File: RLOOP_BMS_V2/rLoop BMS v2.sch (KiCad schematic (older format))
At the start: 2 parts

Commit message: Footprint work
starting to assign footprints to parts
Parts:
- R3, R4: footprint (none) -> Resistors_SMD:R_0603
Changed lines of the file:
@@
 F 0 "R3" V 6100 2550 50  0000 C CNN
 F 1 "10R / 0.125W / 1% / SMD 0603" V 6300 2800 50  0000 C CNN
-F 2 "" V 6130 2600 50  0001 C CNN
+F 2 "Resistors_SMD:R_0603" V 6130 2600 50  0001 C CNN
 F 3 "" H 6200 2600 50  0001 C CNN
 	1    6200 2600
@@
 F 0 "R4" V 6100 4450 50  0000 C CNN
 F 1 "10R / 0.125W / 1% / SMD 0603" V 6300 5050 50  0000 C CNN
-F 2 "" V 6130 4500 50  0001 C CNN
+F 2 "Resistors_SMD:R_0603" V 6130 4500 50  0001 C CNN
 F 3 "" H 6200 4500 50  0001 C CNN
 	1    6200 4500

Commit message: more PCB layout work
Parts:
- added R95: 10R / 0.125W / 1% / SMD 0603, Resistors_SMD:R_0603, symbol R
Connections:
- net Batt Conn/Cell_0: now also R95.1
- new net CONTROLLER 1/GND: R95.2
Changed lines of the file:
@@
 	10150 1500 9200 1500
-Wire Wire Line
-	9200 1500 9200 1600
 Wire Wire Line
 	9200 1600 10150 1600
@@
 Connection ~ 9900 2600
 Wire Wire Line
-	6000 7200 6900 7200
-Wire Wire Line
 	6900 7200 6900 6350
 Wire Wire Line
@@
 	6050 2350 6050 2900
 Connection ~ 6050 2600
+$Comp
+L R R95
+U 1 1 591DF6A5
+P 6450 7200
+F 0 "R95" V 6350 7150 50  0000 C CNN
+F 1 "10R / 0.125W / 1% / SMD 0603" V 6550 7000 50  0000 C CNN
+F 2 "Resistors_SMD:R_0603" V 6380 7200 50  0001 C CNN
+F 3 "" H 6450 7200 50  0001 C CNN
+	1    6450 7200
+	0    1    1    0
+$EndComp
+Wire Wire Line
+	6000 7200 6300 7200
+Wire Wire Line
+	6600 7200 6900 7200
 $EndSCHEMATC

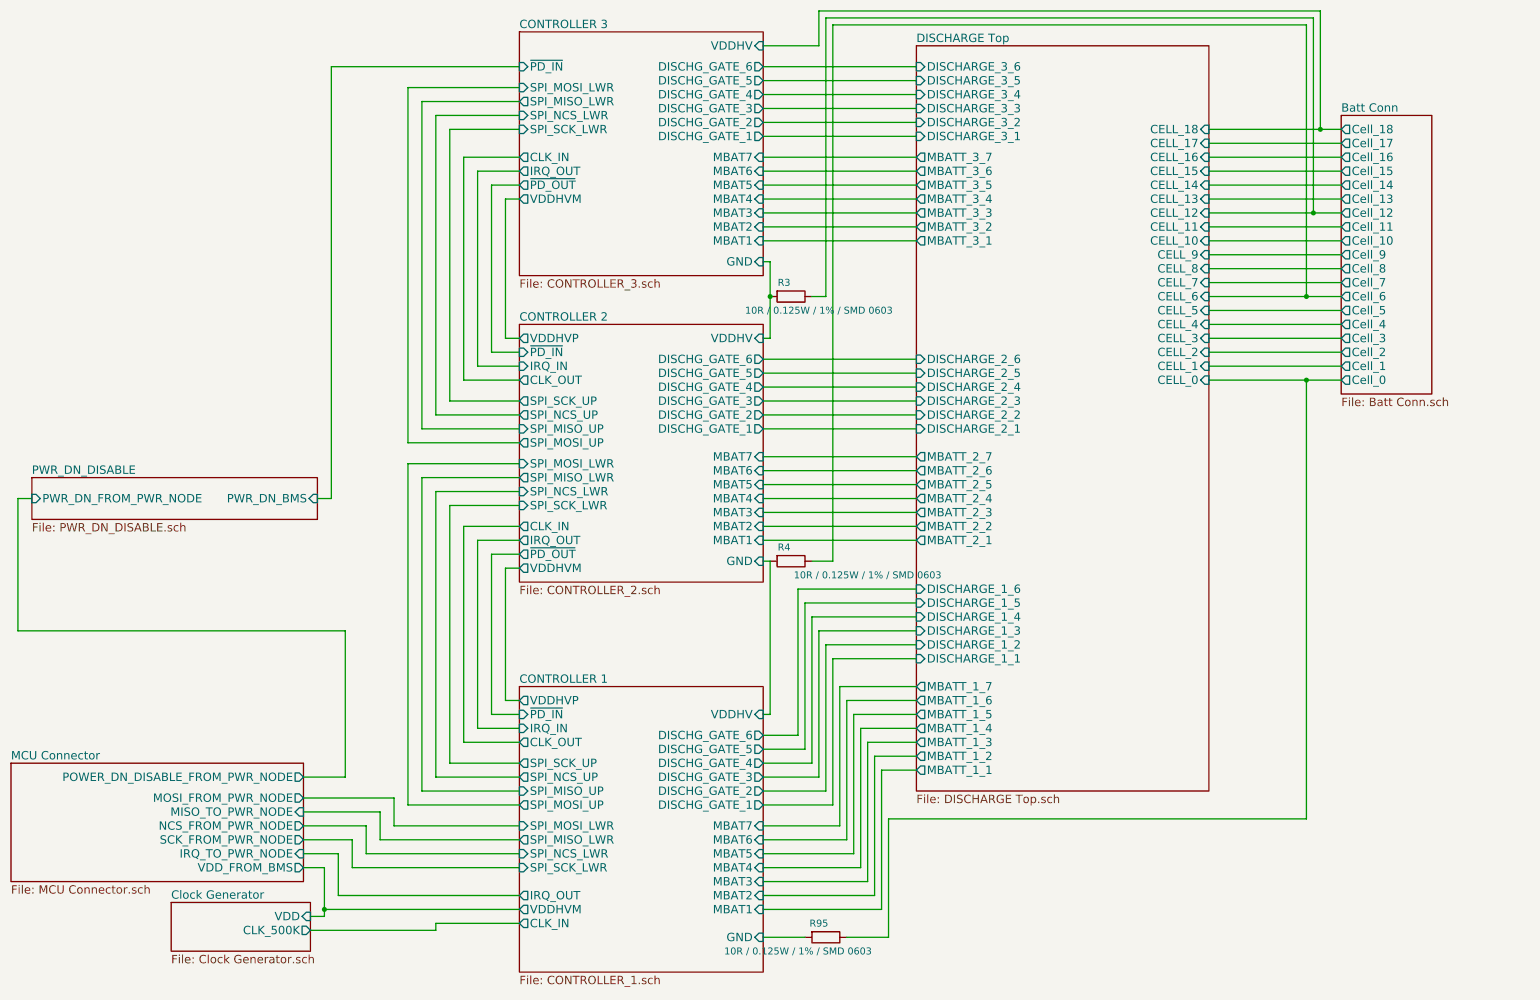
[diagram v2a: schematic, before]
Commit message: WIP
See if it's even possible
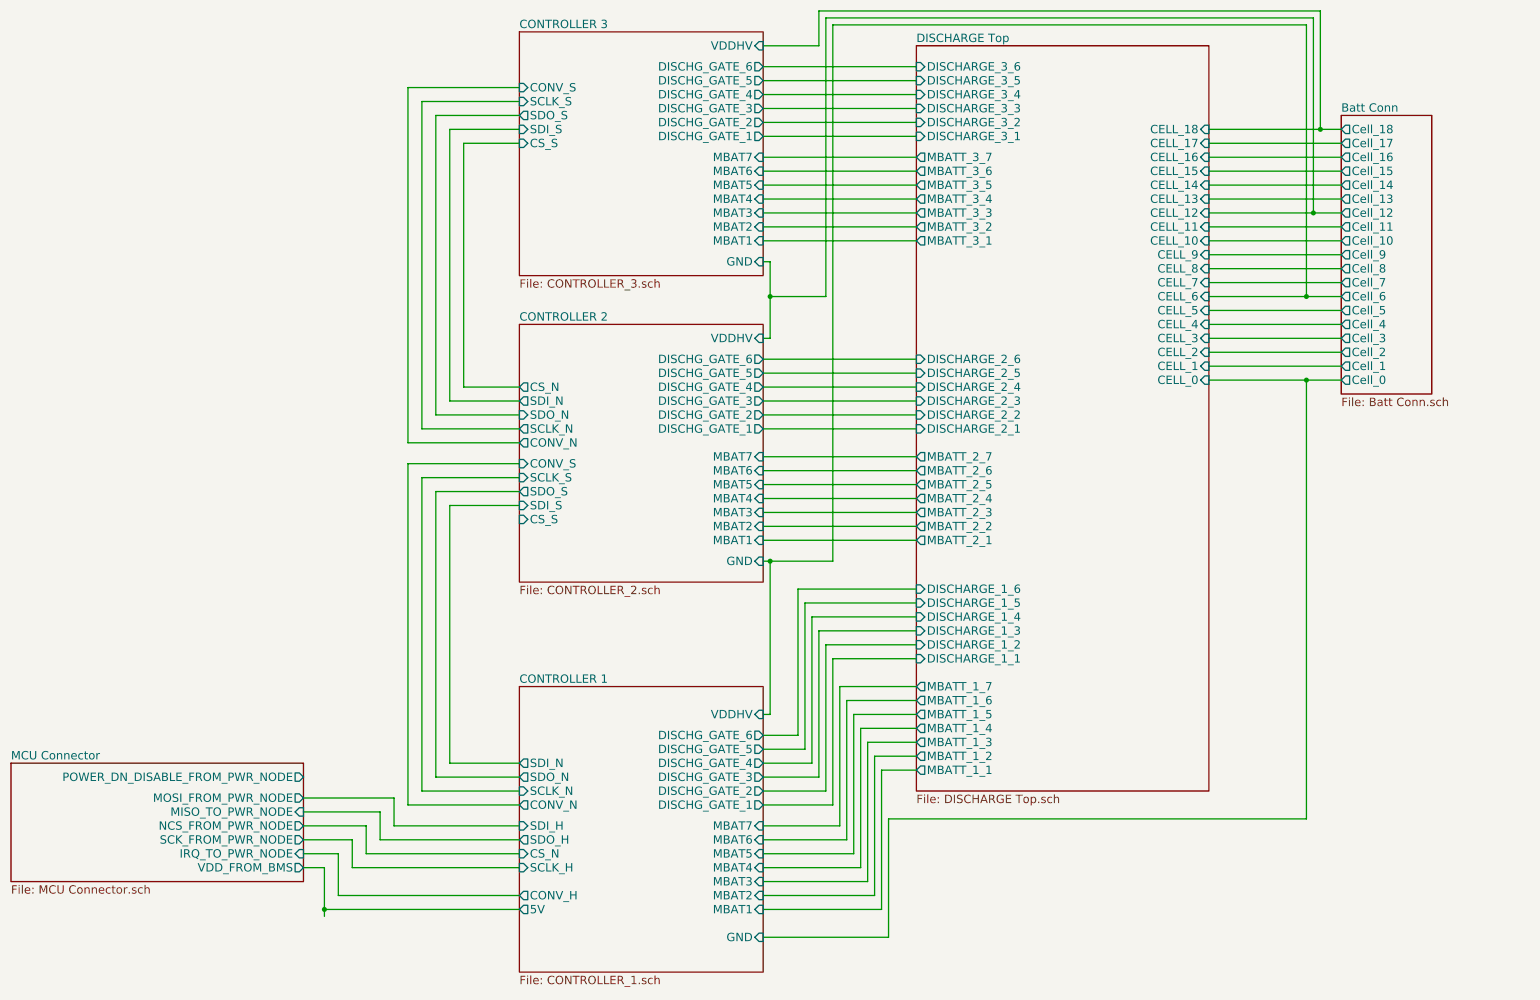
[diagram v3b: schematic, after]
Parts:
- removed R3, R4, R95: 10R / 0.125W / 1% / SMD 0603, Resistors_SMD:R_0603, symbol R
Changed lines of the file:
@@
 $Descr A4 11693 8268
 encoding utf-8
-Sheet 1 9
+Sheet 1 7
 Title ""
 Date ""
@@
 Comment4 ""
 $EndDescr
-$Sheet
-S 1750 6950 1000 350
-U 590C13C3
-F0 "Clock Generator" 60
-F1 "Clock Generator.sch" 60
-F2 "CLK_500K" O R 2750 7150 60
-F3 "VDD" I R 2750 7050 60
-$EndSheet
 $Sheet
 S 600  5950 2100 850
@@
 F7 "POWER_DN_DISABLE_FROM_PWR_NODE" O R 2700 6050 60
 F8 "VDD_FROM_BMS" O R 2700 6700 60
-$EndSheet
-$Sheet
-S 750  3900 2050 300
-U 590C2114
-F0 "PWR_DN_DISABLE" 60
-F1 "PWR_DN_DISABLE.sch" 60
-F2 "PWR_DN_FROM_PWR_NODE" I L 750 4050 60
-F3 "PWR_DN_BMS" I R 2800 4050 60
 $EndSheet
 $Sheet
@@
 F19 "Cell_17" O L 10150 1500 60
 F20 "Cell_18" O L 10150 1400 60
-$EndSheet
-$Sheet
-S 4250 2800 1750 1850
-U 590D87FF
-F0 "CONTROLLER 2" 60
-F1 "CONTROLLER_2.sch" 60
-F2 "MBAT1" I R 6000 4350 60
-F3 "MBAT2" I R 6000 4250 60
-F4 "MBAT3" I R 6000 4150 60
-F5 "MBAT4" I R 6000 4050 60
-F6 "MBAT5" I R 6000 3950 60
-F7 "MBAT6" I R 6000 3850 60
-F8 "MBAT7" I R 6000 3750 60
-F9 "DISCHG_GATE_1" O R 6000 3550 60
-F10 "DISCHG_GATE_2" O R 6000 3450 60
-F11 "DISCHG_GATE_3" O R 6000 3350 60
-F12 "DISCHG_GATE_4" O R 6000 3250 60
-F13 "DISCHG_GATE_5" O R 6000 3150 60
-F14 "DISCHG_GATE_6" O R 6000 3050 60
-F15 "~PD_IN" I L 4250 3000 60
-F16 "~PD_OUT" O L 4250 4450 60
-F17 "CLK_IN" O L 4250 4250 60
-F18 "CLK_OUT" O L 4250 3200 60
-F19 "SPI_NCS_LWR" I L 4250 4000 60
-F20 "SPI_SCK_LWR" I L 4250 4100 60
-F21 "SPI_MOSI_LWR" I L 4250 3800 60
-F22 "SPI_MISO_LWR" O L 4250 3900 60
-F23 "IRQ_IN" I L 4250 3100 60
-F24 "IRQ_OUT" O L 4250 4350 60
-F25 "SPI_MISO_UP" I L 4250 3550 60
-F26 "SPI_SCK_UP" O L 4250 3350 60
-F27 "SPI_NCS_UP" O L 4250 3450 60
-F28 "VDDHVM" O L 4250 4550 60
-F29 "VDDHVP" O L 4250 2900 60
-F30 "SPI_MOSI_UP" O L 4250 3650 60
-F31 "VDDHV" I R 6000 2900 60
-F32 "GND" I R 6000 4500 60
-$EndSheet
-$Sheet
-S 4250 5400 1750 2050
-U 590D88AD
-F0 "CONTROLLER 1" 60
-F1 "CONTROLLER_1.sch" 60
-F2 "MBAT1" I R 6000 7000 60
-F3 "MBAT2" I R 6000 6900 60
-F4 "MBAT3" I R 6000 6800 60
-F5 "MBAT4" I R 6000 6700 60
-F6 "MBAT5" I R 6000 6600 60
-F7 "MBAT6" I R 6000 6500 60
-F8 "MBAT7" I R 6000 6400 60
-F9 "DISCHG_GATE_1" O R 6000 6250 60
-F10 "DISCHG_GATE_2" O R 6000 6150 60
-F11 "DISCHG_GATE_3" O R 6000 6050 60
-F12 "DISCHG_GATE_4" O R 6000 5950 60
-F13 "DISCHG_GATE_5" O R 6000 5850 60
-F14 "DISCHG_GATE_6" O R 6000 5750 60
-F15 "~PD_IN" I L 4250 5600 60
-F16 "CLK_IN" O L 4250 7100 60
-F17 "CLK_OUT" O L 4250 5800 60
-F18 "SPI_NCS_LWR" I L 4250 6600 60
-F19 "SPI_SCK_LWR" I L 4250 6700 60
-F20 "SPI_MOSI_LWR" I L 4250 6400 60
-F21 "SPI_MISO_LWR" O L 4250 6500 60
-F22 "IRQ_IN" I L 4250 5700 60
-F23 "IRQ_OUT" O L 4250 6900 60
-F24 "SPI_MISO_UP" I L 4250 6150 60
-F25 "SPI_SCK_UP" O L 4250 5950 60
-F26 "SPI_NCS_UP" O L 4250 6050 60
-F27 "VDDHVP" O L 4250 5500 60
-F28 "SPI_MOSI_UP" O L 4250 6250 60
-F29 "VDDHVM" O L 4250 7000 60
-F30 "VDDHV" I R 6000 5600 60
-F31 "GND" I R 6000 7200 60
-$EndSheet
-$Sheet
-S 4250 700  1750 1750
-U 590C6B15
-F0 "CONTROLLER 3" 60
-F1 "CONTROLLER_3.sch" 60
-F2 "MBAT1" I R 6000 2200 60
-F3 "MBAT2" I R 6000 2100 60
-F4 "MBAT3" I R 6000 2000 60
-F5 "MBAT4" I R 6000 1900 60
-F6 "MBAT5" I R 6000 1800 60
-F7 "MBAT6" I R 6000 1700 60
-F8 "MBAT7" I R 6000 1600 60
-F9 "DISCHG_GATE_1" O R 6000 1450 60
-F10 "DISCHG_GATE_2" O R 6000 1350 60
-F11 "DISCHG_GATE_3" O R 6000 1250 60
-F12 "DISCHG_GATE_4" O R 6000 1150 60
-F13 "DISCHG_GATE_5" O R 6000 1050 60
-F14 "DISCHG_GATE_6" O R 6000 950 60
-F15 "~PD_IN" I L 4250 950 60
-F16 "~PD_OUT" O L 4250 1800 60
-F17 "CLK_IN" O L 4250 1600 60
-F18 "SPI_NCS_LWR" I L 4250 1300 60
-F19 "SPI_SCK_LWR" I L 4250 1400 60
-F20 "SPI_MOSI_LWR" I L 4250 1100 60
-F21 "SPI_MISO_LWR" O L 4250 1200 60
-F22 "IRQ_OUT" O L 4250 1700 60
-F23 "VDDHVM" O L 4250 1900 60
-F24 "VDDHV" I R 6000 800 60
-F25 "GND" I R 6000 2350 60
 $EndSheet
 $Sheet
@@
 F59 "CELL_18" I R 9200 1400 60
 $EndSheet
-$Comp
-L R R3
-U 1 1 59153F46
-P 6200 2600
-F 0 "R3" V 6100 2550 50  0000 C CNN
-F 1 "10R / 0.125W / 1% / SMD 0603" V 6300 2800 50  0000 C CNN
-F 2 "Resistors_SMD:R_0603" V 6130 2600 50  0001 C CNN
-F 3 "" H 6200 2600 50  0001 C CNN
-	1    6200 2600
-	0    1    1    0
-$EndComp
-$Comp
-L R R4
-U 1 1 59158071
-P 6200 4500
-F 0 "R4" V 6100 4450 50  0000 C CNN
-F 1 "10R / 0.125W / 1% / SMD 0603" V 6300 5050 50  0000 C CNN
-F 2 "Resistors_SMD:R_0603" V 6130 4500 50  0001 C CNN
-F 3 "" H 6200 4500 50  0001 C CNN
-	1    6200 4500
-	0    1    1    0
-$EndComp
-Wire Wire Line
-	4250 2900 4150 2900
-Wire Wire Line
-	4150 2900 4150 1900
-Wire Wire Line
-	4150 1900 4250 1900
-Wire Wire Line
-	4250 3000 4050 3000
-Wire Wire Line
-	4050 3000 4050 1800
-Wire Wire Line
-	4050 1800 4250 1800
-Wire Wire Line
-	4250 3100 3950 3100
-Wire Wire Line
-	3950 3100 3950 1700
-Wire Wire Line
-	3950 1700 4250 1700
 Wire Wire Line
 	3750 1400 4250 1400
 Wire Wire Line
-	4250 1600 3850 1600
-Wire Wire Line
-	3850 1600 3850 3200
-Wire Wire Line
-	3850 3200 4250 3200
-Wire Wire Line
 	4250 3350 3750 3350
 Wire Wire Line
@@
 	3450 3650 4250 3650
 Wire Wire Line
-	4250 950  2900 950
-Wire Wire Line
-	2900 950  2900 4050
-Wire Wire Line
-	2900 4050 2800 4050
-Wire Wire Line
-	4250 5500 4150 5500
-Wire Wire Line
-	4150 5500 4150 4550
-Wire Wire Line
-	4150 4550 4250 4550
-Wire Wire Line
-	4250 5600 4050 5600
-Wire Wire Line
-	4050 5600 4050 4450
-Wire Wire Line
-	4050 4450 4250 4450
-Wire Wire Line
-	4250 5700 3950 5700
-Wire Wire Line
-	3950 5700 3950 4350
-Wire Wire Line
-	3950 4350 4250 4350
-Wire Wire Line
-	4250 5800 3850 5800
-Wire Wire Line
-	3850 5800 3850 4250
-Wire Wire Line
-	3850 4250 4250 4250
-Wire Wire Line
 	3750 5950 4250 5950
 Wire Wire Line
@@
 	3350 6200 2700 6200
 Wire Wire Line
-	2700 6050 3000 6050
-Wire Wire Line
-	3000 6050 3000 5000
-Wire Wire Line
-	3000 5000 650  5000
-Wire Wire Line
-	650  5000 650  4050
-Wire Wire Line
-	650  4050 750  4050
-Wire Wire Line
 	9200 1400 10150 1400
 Wire Wire Line
@@
 	7100 2200 6000 2200
 Wire Wire Line
-	6000 4500 6050 4500
+	6000 4500 6500 4500
 Wire Wire Line
 	6050 4500 6050 5600
@@
 Connection ~ 10000 1400
 Wire Wire Line
-	6350 2600 6450 2600
+	6050 2600 6450 2600
 Wire Wire Line
 	6450 2600 6450 600
 Wire Wire Line
 	6450 600  9950 600
-Wire Wire Line
-	6350 4500 6500 4500
 Wire Wire Line
 	6500 4500 6500 650
@@
 	9950 600  9950 2000
 Connection ~ 9950 2000
-Wire Wire Line
-	2850 7050 2750 7050
 Connection ~ 2850 7000
-Wire Wire Line
-	2750 7150 3650 7150
-Wire Wire Line
-	3650 7150 3650 7100
-Wire Wire Line
-	3650 7100 4250 7100
 Wire Wire Line
 	6050 2350 6050 2900
 Connection ~ 6050 2600
-$Comp
-L R R95
-U 1 1 591DF6A5
-P 6450 7200
-F 0 "R95" V 6350 7150 50  0000 C CNN
-F 1 "10R / 0.125W / 1% / SMD 0603" V 6550 7000 50  0000 C CNN
-F 2 "Resistors_SMD:R_0603" V 6380 7200 50  0001 C CNN
-F 3 "" H 6450 7200 50  0001 C CNN
-	1    6450 7200
-	0    1    1    0
-$EndComp
-Wire Wire Line
-	6000 7200 6300 7200
-Wire Wire Line
-	6600 7200 6900 7200
+Wire Wire Line
+	6000 7200 6900 7200
+Connection ~ 6050 4500
+$Sheet
+S 4250 700  1750 1750
+U 590C6B15
+F0 "CONTROLLER 3" 60
+F1 "CONTROLLER_3.sch" 60
+F2 "MBAT1" I R 6000 2200 60
+F3 "MBAT2" I R 6000 2100 60
+F4 "MBAT3" I R 6000 2000 60
+F5 "MBAT4" I R 6000 1900 60
+F6 "MBAT5" I R 6000 1800 60
+F7 "MBAT6" I R 6000 1700 60
+F8 "MBAT7" I R 6000 1600 60
+F9 "DISCHG_GATE_1" O R 6000 1450 60
+F10 "DISCHG_GATE_2" O R 6000 1350 60
+F11 "DISCHG_GATE_3" O R 6000 1250 60
+F12 "DISCHG_GATE_4" O R 6000 1150 60
+F13 "DISCHG_GATE_5" O R 6000 1050 60
+F14 "DISCHG_GATE_6" O R 6000 950 60
+F15 "CS_S" I L 4250 1500 60
+F16 "SDO_S" O L 4250 1300 60
+F17 "SDI_S" I L 4250 1400 60
+F18 "CONV_S" I L 4250 1100 60
+F19 "SCLK_S" I L 4250 1200 60
+F20 "VDDHV" I R 6000 800 60
+F21 "GND" I R 6000 2350 60
+$EndSheet
+$Sheet
+S 4250 2800 1750 1850
+U 590D87FF
+F0 "CONTROLLER 2" 60
+F1 "CONTROLLER_2.sch" 60
+F2 "MBAT1" I R 6000 4350 60
+F3 "MBAT2" I R 6000 4250 60
+F4 "MBAT3" I R 6000 4150 60
+F5 "MBAT4" I R 6000 4050 60
+F6 "MBAT5" I R 6000 3950 60
+F7 "MBAT6" I R 6000 3850 60
+F8 "MBAT7" I R 6000 3750 60
+F9 "DISCHG_GATE_1" O R 6000 3550 60
+F10 "DISCHG_GATE_2" O R 6000 3450 60
+F11 "DISCHG_GATE_3" O R 6000 3350 60
+F12 "DISCHG_GATE_4" O R 6000 3250 60
+F13 "DISCHG_GATE_5" O R 6000 3150 60
+F14 "DISCHG_GATE_6" O R 6000 3050 60
+F15 "SDO_S" O L 4250 4000 60
+F16 "SDI_S" I L 4250 4100 60
+F17 "CONV_S" I L 4250 3800 60
+F18 "SCLK_S" I L 4250 3900 60
+F19 "SCLK_N" O L 4250 3550 60
+F20 "SDI_N" O L 4250 3350 60
+F21 "SDO_N" I L 4250 3450 60
+F22 "CONV_N" O L 4250 3650 60
+F23 "VDDHV" I R 6000 2900 60
+F24 "GND" I R 6000 4500 60
+F25 "CS_S" I L 4250 4200 60
+F26 "CS_N" O L 4250 3250 60
+$EndSheet
+$Sheet
+S 4250 5400 1750 2050
+U 590D88AD
+F0 "CONTROLLER 1" 60
+F1 "CONTROLLER_1.sch" 60
+F2 "MBAT1" I R 6000 7000 60
+F3 "MBAT2" I R 6000 6900 60
+F4 "MBAT3" I R 6000 6800 60
+F5 "MBAT4" I R 6000 6700 60
+F6 "MBAT5" I R 6000 6600 60
+F7 "MBAT6" I R 6000 6500 60
+F8 "MBAT7" I R 6000 6400 60
+F9 "DISCHG_GATE_1" O R 6000 6250 60
+F10 "DISCHG_GATE_2" O R 6000 6150 60
+F11 "DISCHG_GATE_3" O R 6000 6050 60
+F12 "DISCHG_GATE_4" O R 6000 5950 60
+F13 "DISCHG_GATE_5" O R 6000 5850 60
+F14 "DISCHG_GATE_6" O R 6000 5750 60
+F15 "CS_N" I L 4250 6600 60
+F16 "SCLK_H" I L 4250 6700 60
+F17 "SDI_H" I L 4250 6400 60
+F18 "SDO_H" O L 4250 6500 60
+F19 "CONV_H" O L 4250 6900 60
+F20 "SCLK_N" I L 4250 6150 60
+F21 "SDI_N" O L 4250 5950 60
+F22 "SDO_N" O L 4250 6050 60
+F23 "CONV_N" O L 4250 6250 60
+F24 "5V" O L 4250 7000 60
+F25 "VDDHV" I R 6000 5600 60
+F26 "GND" I R 6000 7200 60
+$EndSheet
+Wire Wire Line
+	4250 3250 3850 3250
+Wire Wire Line
+	3850 3250 3850 1500
+Wire Wire Line
+	3850 1500 4250 1500
 $EndSCHEMATC

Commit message: Ti BMS WIP
Getting there. Need to add temp sensors, fan control, and an LDO for the
SPI ISO supply.
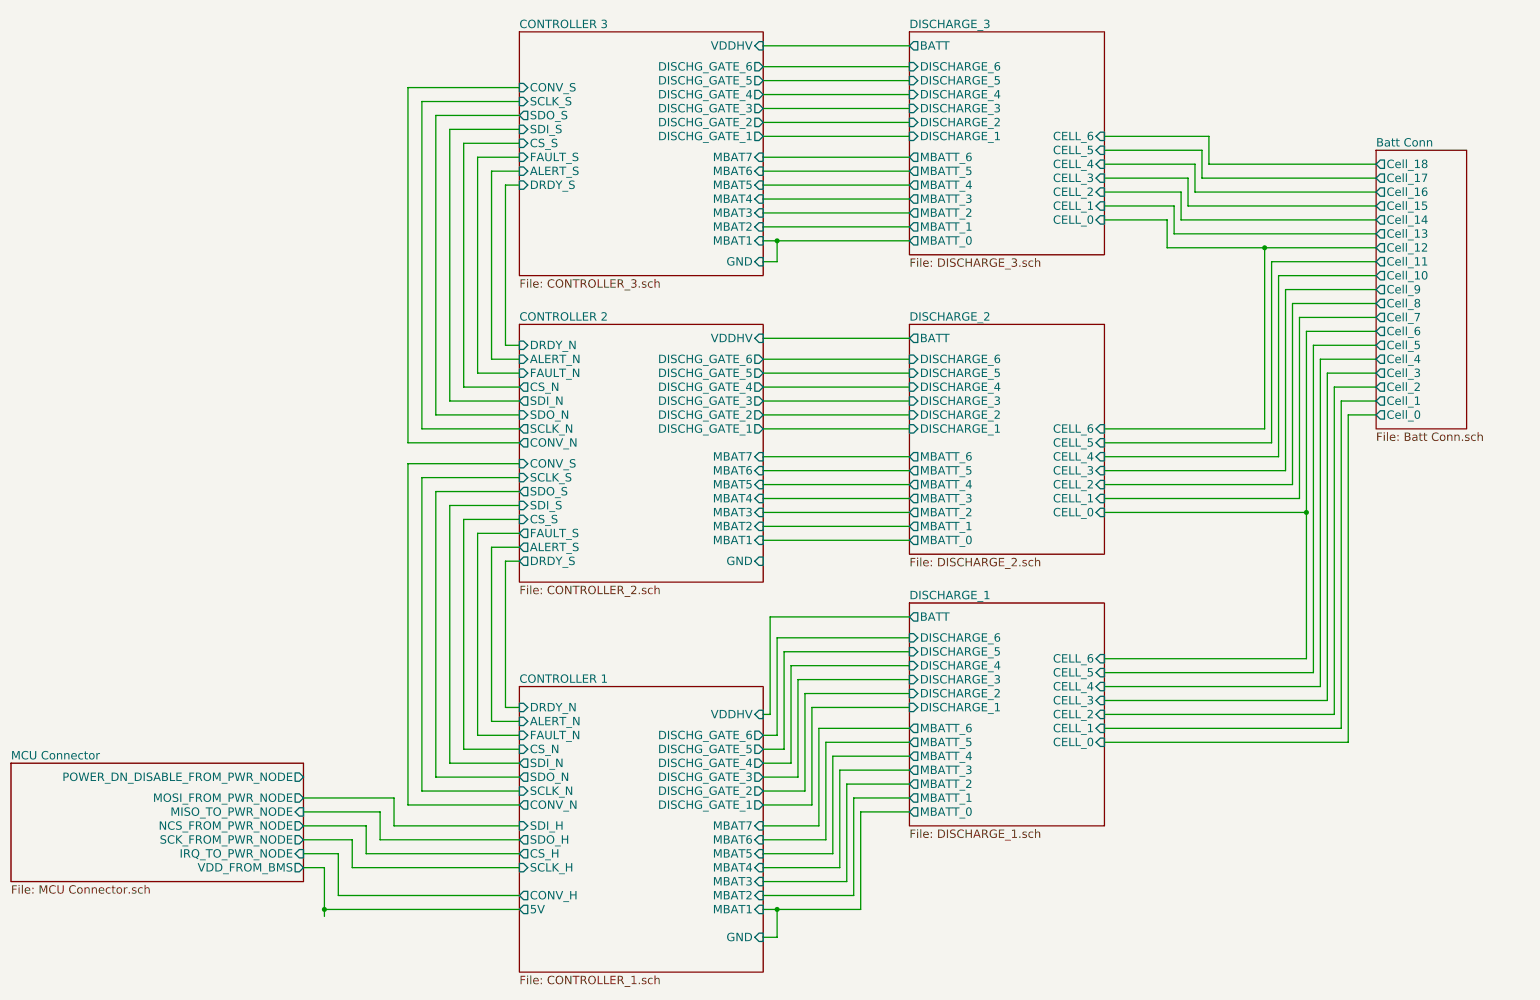
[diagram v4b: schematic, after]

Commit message: More BMS v2.5 WIP
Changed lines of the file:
@@
 $Descr A4 11693 8268
 encoding utf-8
-Sheet 1 9
+Sheet 1 10
 Title ""
 Date ""
@@
 	3450 6250 4250 6250
 Wire Wire Line
-	2700 6700 2850 6700
-Wire Wire Line
-	2850 6700 2850 7050
-Wire Wire Line
-	2850 7000 4250 7000
-Wire Wire Line
 	4250 6900 2950 6900
 Wire Wire Line
@@
 Wire Wire Line
 	3350 6200 2700 6200
-Connection ~ 2850 7000
 $Sheet
 S 4250 700  1750 1750
@@
 	9150 1750 10400 1750
 Wire Wire Line
-	10400 1650 9200 1650
-Wire Wire Line
-	9200 1650 9200 1450
+	9200 1650 10400 1650
+Wire Wire Line
+	9200 550  9200 1650
 Wire Wire Line
 	9200 1450 8450 1450
@@
 Wire Wire Line
 	4150 2950 4250 2950
+$Sheet
+S 950  1950 1550 1200
+U 592F4D0C
+F0 "ISO POWER" 60
+F1 "ISO Power.sch" 60
+F2 "ISO_GND" O R 2500 2400 60
+F3 "BATT" O R 2500 2250 60
+F4 "5V_ISO" O R 2500 2650 60
+$EndSheet
+Wire Wire Line
+	2550 550  2550 2250
+Wire Wire Line
+	2550 2250 2500 2250
+Wire Wire Line
+	2550 550  9200 550
+Connection ~ 9200 1450
+Wire Wire Line
+	2500 2400 2600 2400
+Wire Wire Line
+	2600 2400 2600 600
+Wire Wire Line
+	2600 600  10300 600
+Wire Wire Line
+	10300 600  10300 3450
+Connection ~ 10300 3450
+Wire Wire Line
+	2500 2650 2800 2650
+Wire Wire Line
+	2800 2650 2800 6700
+Wire Wire Line
+	2800 6700 2700 6700
 $EndSCHEMATC
